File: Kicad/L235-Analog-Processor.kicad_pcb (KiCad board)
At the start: 2 copper layers, 110 x 110 mm, 336 parts, among them J1 Input A, J10 Half Wave A + -B, J11 Inverted Out B, J12 CV Select, J13 CV Select, J14 Conn_01x20_Pin, J15 Inverted Out A, J16 Full-Wave Rectifier A, J17 Half-Wave Rectifier A, J18 √(A²+B²), J19 Conn_01x20_Socket, J2 Input B, J20 Conn_01x05_Socket, J21 Conn_01x05_Pin, J22 Conn_01x05_Socket, J23 Conn_01x05_Pin, J3 Function IN, J4 ( 10A / |B| ) / ( A * B / 10 ), J5 Output F(x), J6 Power, J7 Full-Wave Rectifier B, J8 A - B, J9 Negative Half-Wave Rectifier B, U1 TL082, U10 TL082, U11 TL082, U12 TL082, U13 TL084, U14 RC4580, U15 TL082, U16 AD633ARZ-RL, U17 TL082, U18 LM4040DBZ-10, U19 74HC148, U2 TL082, U20 LM339, U21 LM339, U22 CD4051, U23 CD4051, U24 CD4051, U25 CD4051, U26 CD4051, U27 CD4051, U28 CD4051, U29 LM339, U3 TL082, U30 LM339, U31 74HC148, U32 DG4051E, U33 DG4051E, U34 DG4051E, U35 DG4051E, U36 LM78M05_TO252, U37 TL082, U39 CD4051, U4 TL082, U40 CD4051, U5 TL082, U6 TL082, U7 TL082, U8 TL082, U9 TL082

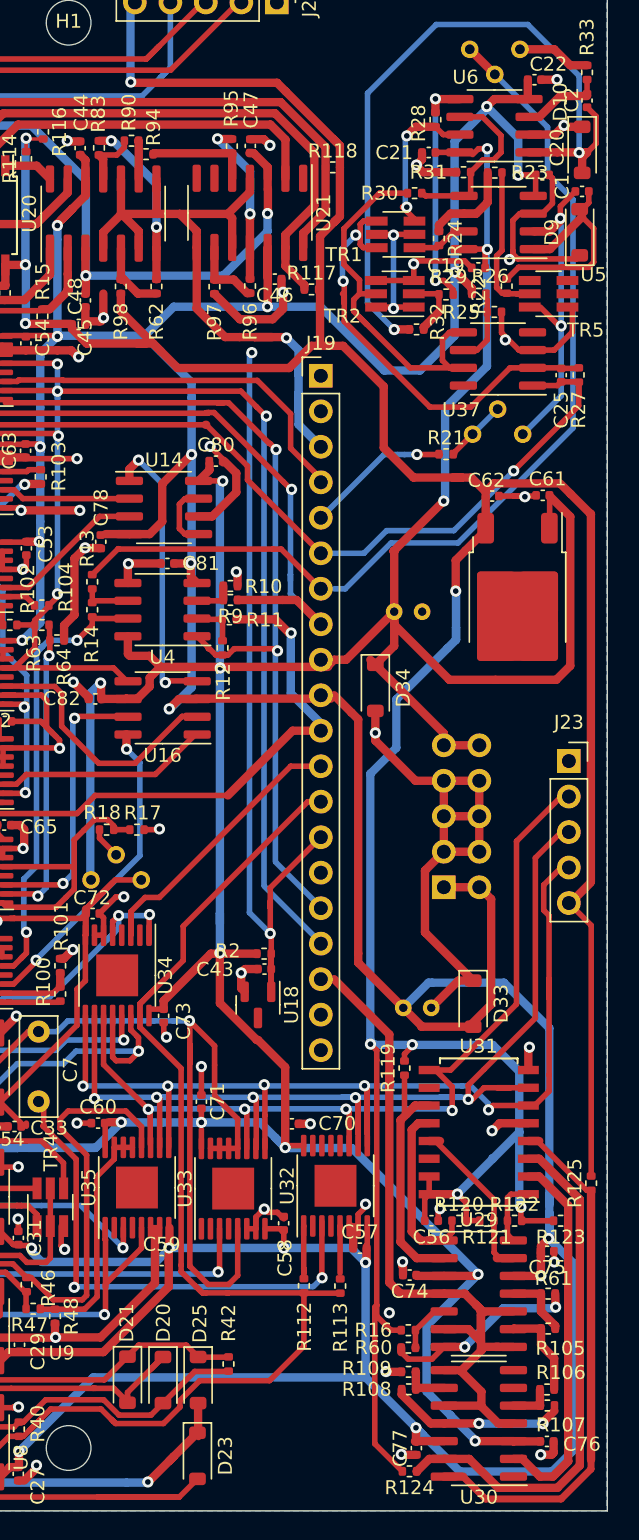
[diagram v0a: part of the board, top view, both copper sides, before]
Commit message: Flipped +- comparators to fix H/L order to actually work with logic table
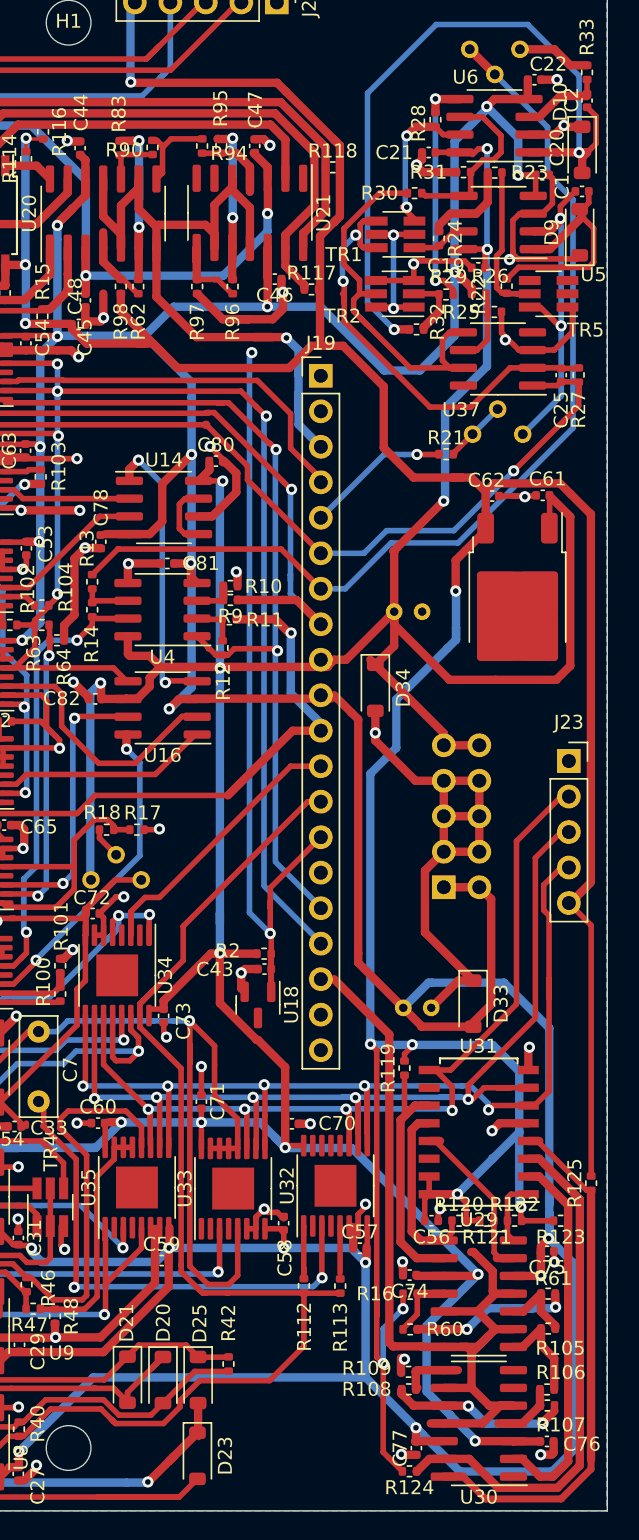
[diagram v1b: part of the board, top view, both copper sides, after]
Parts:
- moved R94 4.06 mm to (203.7, 39.8), turned to 90 degrees
- moved R16 2.60 mm to (218.5, 121.9)
- moved R90 1.58 mm to (200.1, 39.9), turned to -90 degrees
- moved R83 1.48 mm to (197.8, 39.9)
- moved R60 1.32 mm to (218.5, 124.5), turned to 180 degrees
- moved R62 1.30 mm to (199.1, 49.8)
- moved R96 1.24 mm to (205.8, 49.8)
- moved R97 1.23 mm to (203.3, 49.8)
- moved R95 0.76 mm to (205.0, 39.8)
- moved C47 0.32 mm to (207.4, 39.8)
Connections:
- R105 pad 1: Net-(U29D-+) -> Net-(U29D--)
- R105 pad 2: Net-(U29C-+) -> Net-(U29C--)
- R106 pad 1: Net-(U30A-+) -> Net-(U30A--)
- R106 pad 2: Net-(U29D-+) -> Net-(U29D--)
- R107 pad 1: Net-(U30C-+) -> Net-(U30C--)
- R107 pad 2: Net-(U30A-+) -> Net-(U30A--)
- R108 pad 1: Net-(U30D-+) -> Net-(U30D--)
- R108 pad 2: Net-(U30C-+) -> Net-(U30C--)
- R109 pad 2: Net-(U30D-+) -> Net-(U30D--)
- R16 pad 1: Net-(U29A-+) -> Net-(U29A--)
- R60 pad 1: Net-(U29B-+) -> Net-(U29B--)
- R60 pad 2: Net-(U29A-+) -> Net-(U29A--)
- R61 pad 1: Net-(U29C-+) -> Net-(U29C--)
- R61 pad 2: Net-(U29B-+) -> Net-(U29B--)
- R62 pad 1: Net-(U20B-+) -> Net-(U20B--)
- R62 pad 2: Net-(U20A-+) -> Net-(U20A--)
- R83 pad 1: Net-(U20C-+) -> Net-(U20C--)
- R83 pad 2: Net-(U20B-+) -> Net-(U20B--)
- R90 pad 1: Net-(U20D-+) -> Net-(U20D--)
- R90 pad 2: Net-(U20C-+) -> Net-(U20C--)
- R94 pad 1: Net-(U21A-+) -> Net-(U21A--)
- R94 pad 2: Net-(U20D-+) -> Net-(U20D--)
- R95 pad 1: Net-(U21C-+) -> Net-(U21C--)
- R95 pad 2: Net-(U21A-+) -> Net-(U21A--)
- R96 pad 1: Net-(U21D-+) -> Net-(U21D--)
- R96 pad 2: Net-(U21C-+) -> Net-(U21C--)
- R97 pad 2: Net-(U21D-+) -> Net-(U21D--)
- R98 pad 1: Net-(U20A-+) -> Net-(U20A--)
- U20 pad 10: CV_SELECT -> Net-(U20C--)
- U20 pad 11: Net-(U20C-+) -> CV_SELECT
- U20 pad 4: CV_SELECT -> Net-(U20A--)
- U20 pad 5: Net-(U20A-+) -> CV_SELECT
- U20 pad 6: CV_SELECT -> Net-(U20B--)
- U20 pad 7: Net-(U20B-+) -> CV_SELECT
- U20 pad 8: CV_SELECT -> Net-(U20D--)
- U20 pad 9: Net-(U20D-+) -> CV_SELECT
- U21 pad 10: CV_SELECT -> Net-(U21C--)
- U21 pad 11: Net-(U21C-+) -> CV_SELECT
- U21 pad 4: CV_SELECT -> Net-(U21A--)
- U21 pad 5: Net-(U21A-+) -> CV_SELECT
- U21 pad 8: CV_SELECT -> Net-(U21D--)
- U21 pad 9: Net-(U21D-+) -> CV_SELECT
- U29 pad 10: CV_FUNCTION -> Net-(U29C--)
- U29 pad 11: Net-(U29C-+) -> CV_FUNCTION
- U29 pad 4: CV_FUNCTION -> Net-(U29A--)
- U29 pad 5: Net-(U29A-+) -> CV_FUNCTION
- U29 pad 6: CV_FUNCTION -> Net-(U29B--)
- U29 pad 7: Net-(U29B-+) -> CV_FUNCTION
- U29 pad 8: CV_FUNCTION -> Net-(U29D--)
- U29 pad 9: Net-(U29D-+) -> CV_FUNCTION
- U30 pad 10: CV_FUNCTION -> Net-(U30C--)
- U30 pad 11: Net-(U30C-+) -> CV_FUNCTION
- U30 pad 4: CV_FUNCTION -> Net-(U30A--)
- U30 pad 5: Net-(U30A-+) -> CV_FUNCTION
- U30 pad 8: CV_FUNCTION -> Net-(U30D--)
- U30 pad 9: Net-(U30D-+) -> CV_FUNCTION
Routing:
- net Net-(U29B--): track 0.00 -> 14.6 mm, vias 0 -> 2
- net Net-(U20B--): track 0.00 -> 14.4 mm, vias 0 -> 2
- net Net-(U29B-+): track 14.3 -> 0.00 mm, vias 2 -> 0
- net Net-(U30C--): track 0.00 -> 13.4 mm, vias 0 -> 2
- net Net-(U30C-+): track 13.0 -> 0.00 mm, vias 2 -> 0
- net Net-(U21C-+): track 12.4 -> 0.00 mm, vias 2 -> 0
- net Net-(U20B-+): track 12.2 -> 0.00 mm, vias 2 -> 0
- net Net-(U21C--): track 0.00 -> 12.0 mm, vias 0 -> 2
- net CV_FUNCTION: track 71.0 -> 80.6 mm
- net CV_SELECT: track 87.3 -> 95.2 mm
- net Net-(U21A-+): track 7.46 -> 0.00 mm
- net Net-(U29D--): track 0.00 -> 7.27 mm
- net Net-(U29D-+): track 6.74 -> 0.00 mm
- net Net-(U20D--): track 0.00 -> 6.52 mm
- net Net-(U21D--): track 0.00 -> 6.30 mm
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
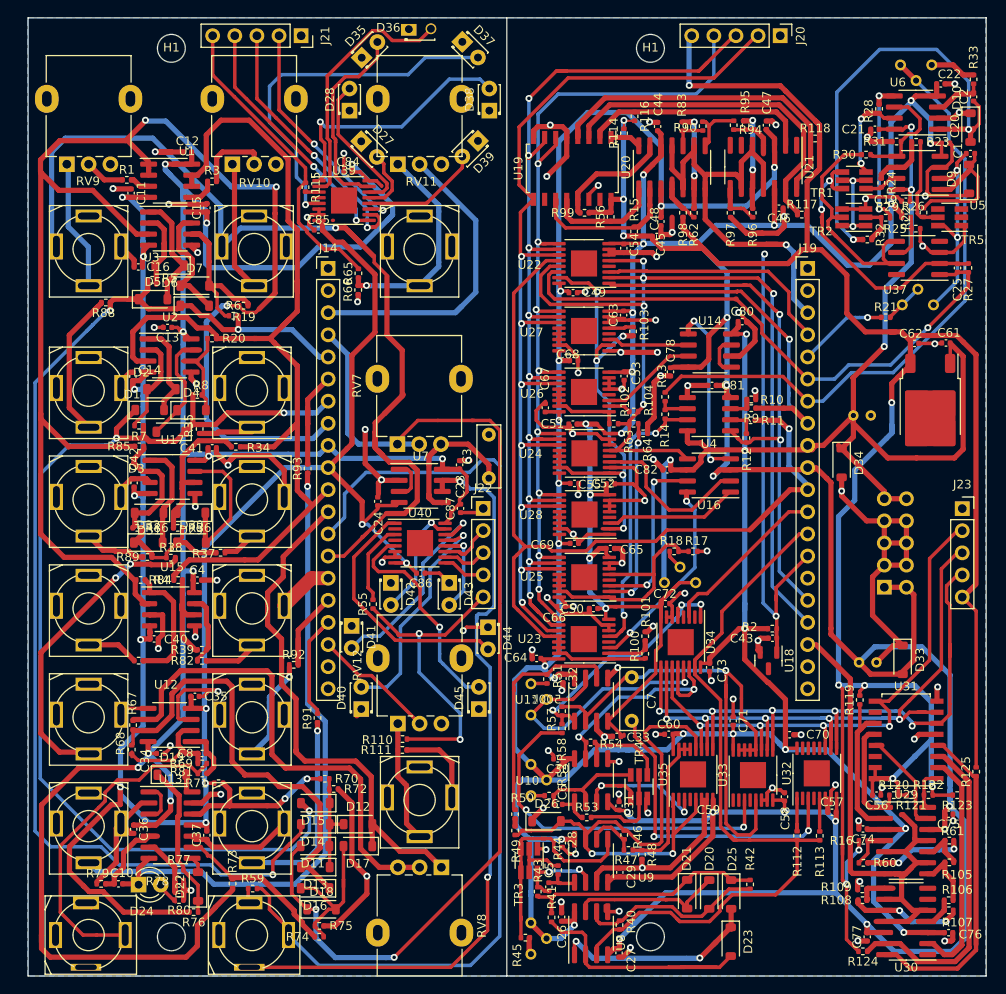
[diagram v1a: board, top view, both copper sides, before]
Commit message: Cleanup trace thickness, text alignment
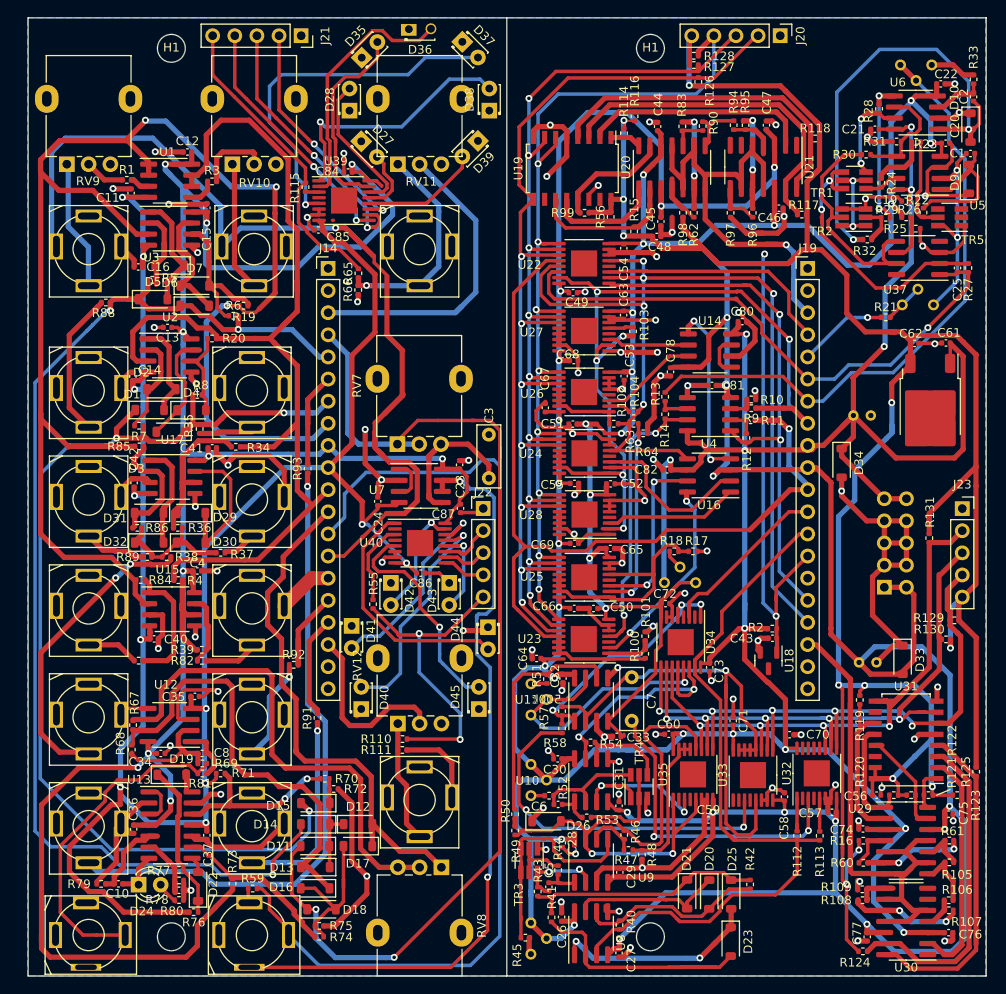
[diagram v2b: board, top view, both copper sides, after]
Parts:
- added R126: 4k7, Resistor_SMD:R_0402_1005Metric, F.Cu at (199.6, 34.8)
- added R127: 4k7, Resistor_SMD:R_0402_1005Metric, F.Cu at (199.1, 32.9)
- added R128: 4k7, Resistor_SMD:R_0402_1005Metric, F.Cu at (199.1, 31.8)
- added R129: 4k7, Resistor_SMD:R_0402_1005Metric, F.Cu at (229.0, 96.6)
- added R130: 4k7, Resistor_SMD:R_0402_1005Metric, F.Cu at (228.0, 98.8)
- added R131: 4k7, Resistor_SMD:R_0402_1005Metric, F.Cu at (226.1, 87.2)
- moved C66 1.51 mm to (185.3, 95.2), turned to 180 degrees
- moved R71 1.14 mm to (144.8, 114.2)
- moved C4 1.05 mm to (142.1, 91.0)
- moved R38 0.49 mm to (138.6, 89.3)
- moved D32 0.10 mm to (136.6, 87.7)
- moved D30 0.05 mm to (141.3, 87.7)
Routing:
- net +5V: track 358.5 -> 380.0 mm, vias 13 -> 14
- net B0: track 72.0 -> 77.3 mm
- net GND: track 469.0 -> 464.1 mm, vias 90 -> 89
- net A2: track 135.6 -> 138.6 mm
- net CV_FUNCTION: track 80.6 -> 82.4 mm
- net A1: track 149.1 -> 147.4 mm
- net Net-(U13D-+): track 19.0 -> 20.6 mm
- net Net-(U30A--): track 4.69 -> 3.60 mm
- net -12V: track 697.7 -> 698.7 mm
- net Net-(U31-7): track 38.6 -> 37.6 mm
- net LED_B5: track 28.9 -> 28.1 mm
- net B: track 228.3 -> 229.1 mm
- net B2: track 79.1 -> 79.9 mm

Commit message: Removed invert jacks for attenuverter + offset knob
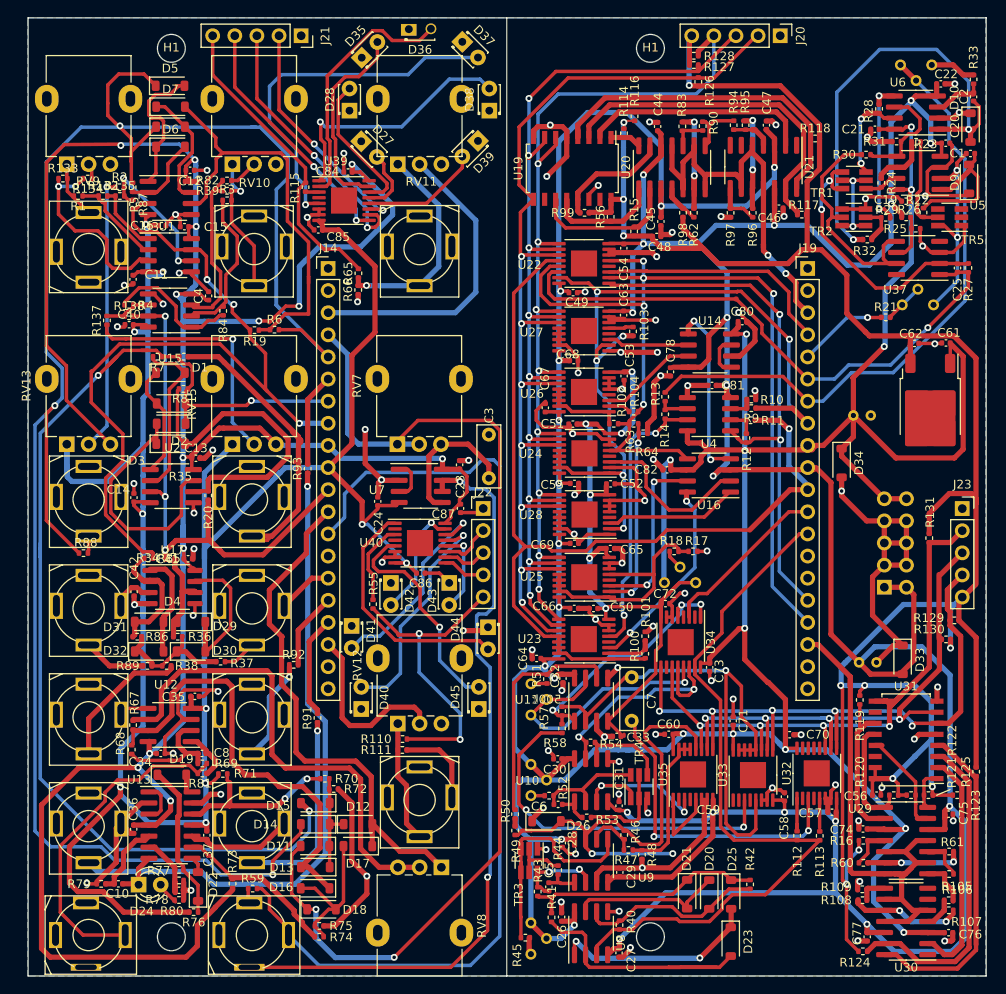
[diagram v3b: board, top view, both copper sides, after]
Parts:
- removed C43: 100nF, Capacitor_SMD:C_0402_1005Metric
- removed J11: Inverted Out B, Custom_Footprints:Cliff_3.5mm_Stereo_Jack
- removed J15: Inverted Out A, Custom_Footprints:Cliff_3.5mm_Stereo_Jack
- removed U18: LM4040DBZ-10, Package_TO_SOT_SMD:SOT-23
- added R132: 100k, Resistor_SMD:R_0402_1005Metric, F.Cu at (131.2, 47.9)
- added R133: 47k, Resistor_SMD:R_0402_1005Metric, F.Cu at (126.7, 45.9)
- added R134: 47k, Resistor_SMD:R_0402_1005Metric, F.Cu at (129.5, 45.9)
- added R135: 100k, Resistor_SMD:R_0402_1005Metric, F.Cu at (133.2, 47.9)
- added R137: 220k, Resistor_SMD:R_0402_1005Metric, F.Cu at (131.7, 62.2)
- added R138: 100k, Resistor_SMD:R_0402_1005Metric, F.Cu at (134.2, 61.7)
- added RV13: 100k, Potentiometer_THT:Potentiometer_Alpha_RD901F-40-00D_Single_Vertical, F.Cu at (127.1, 76.4)
- added RV15: 100k, Potentiometer_THT:Potentiometer_Alpha_RD901F-40-00D_Single_Vertical, F.Cu at (146.1, 76.4)
- R1, R3, R4, R84: value 10k -> 100k
- R2: value 1k -> 220k
- R39: value 10k -> 47k
- R82: value 1k -> 47k
- R87: value 1k -> 100k
- U15: footprint Package_SO:SO-8_3.9x4.9mm_P1.27mm -> Package_SO:SOIC-8_3.9x4.9mm_P1.27mm
- moved R2 90.5 mm to (133.2, 46.9)
- moved R82 55.2 mm to (145.5, 46.1)
- moved R39 52.8 mm to (145.5, 47.3)
- moved R87 52.4 mm to (134.7, 48.9), turned to -90 degrees
- moved C40 36.2 mm to (134.2, 62.7), turned to 0 degrees
- moved U15 34.3 mm to (138.9, 61.0), turned to 180 degrees
- moved R84 32.3 mm to (145.1, 61.1), turned to -90 degrees
- moved R4 32.1 mm to (134.2, 60.4)
- moved C4 31.6 mm to (143.4, 59.4), turned to 90 degrees
- moved R88 28.9 mm to (129.0, 88.9), turned to 0 degrees
- moved D5 24.6 mm to (138.9, 35.2)
- moved D7 20.7 mm to (139.0, 37.6)
- moved D8 20.7 mm to (139.0, 40.0)
- moved R20 18.0 mm to (143.3, 82.3), turned to 90 degrees
- moved C13 15.4 mm to (141.9, 78.0), turned to 0 degrees
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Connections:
- J1 pad TN: 10V REF -> GND
- J14 pad 14: 10V REF -> unconnected-(J14-Pin_14-Pad14)
- J19 pad 14: 10V REF -> unconnected-(J19-Pin_14-Pad14)
- J2 pad TN: 10V REF -> GND
- R1 pad 1: Net-(R1-Pad1) -> Net-(U1A--)
- R1 pad 2: Net-(U1A-+) -> Net-(J1-PadT)
- R2 pad 1: +12V -> Net-(R2-Pad1)
- R2 pad 2: 10V REF -> Net-(U1B--)
- R3 pad 1: Net-(R3-Pad1) -> Net-(J2-PadT)
- R3 pad 2: Net-(U1B-+) -> Net-(U15A--)
- R39 pad 1: Net-(U15B--) -> Net-(U15A-+)
- R39 pad 2: -B -> Net-(J2-PadT)
- R4 pad 1: B -> Net-(R4-Pad1)
- R82 pad 1: Net-(J11-PadT) -> Net-(R82-Pad1)
- R82 pad 2: -B -> Net-(U15A-+)
- R84 pad 1: A -> Net-(U15A--)
- R84 pad 2: -A -> Net-(R4-Pad1)
- R87 pad 1: Net-(J15-PadT) -> Net-(U1B--)
- R87 pad 2: -A -> A
- RV10 pad 2: Net-(R3-Pad1) -> Net-(R82-Pad1)
- RV9 pad 2: Net-(R1-Pad1) -> Net-(R134-Pad1)
- U1 pad 1: A -> Net-(R132-Pad2)
- U1 pad 2: A -> Net-(U1A--)
- U1 pad 5: Net-(U1B-+) -> GND
- U1 pad 6: B -> Net-(U1B--)
- U1 pad 7: B -> A
- U15 pad 1: -A -> Net-(R4-Pad1)
- U15 pad 2: A -> Net-(U15A--)
- U15 pad 3: GND -> Net-(U15A-+)
- U15 pad 4: -12V -> +12V
- U15 pad 7: -B -> B
- U15 pad 8: +12V -> -12V
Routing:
- net 10V REF: track 172.2 -> 0.00 mm, vias 3 -> 0
- net |A|: track 146.9 -> 237.7 mm
- net A: track 274.0 -> 186.2 mm
- net B: track 229.1 -> 172.5 mm, vias 1 -> 4
- net +12V: track 722.7 -> 773.3 mm, vias 34 -> 37
- net GND: track 464.1 -> 427.3 mm, vias 89 -> 91
- net Net-(J7-PadT): track 6.74 -> 42.7 mm
- net Net-(R2-Pad1): track 0.00 -> 31.4 mm, vias 0 -> 1
- net Net-(D7-A): track 18.8 -> 48.8 mm
- net Net-(R137-Pad1): track 0.00 -> 28.8 mm, vias 0 -> 1
- net Net-(D4-A): track 11.5 -> 37.2 mm
- net -12V: track 698.7 -> 722.7 mm, vias 35 -> 34
- net +5V: track 380.0 -> 356.1 mm, vias 14 -> 13
- net Net-(U15A-+): track 0.00 -> 20.1 mm
- net Net-(U1A-+): track 2.30 -> 22.3 mm, vias 0 -> 2
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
